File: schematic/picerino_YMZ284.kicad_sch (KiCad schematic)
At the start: 23 parts, among them CON1 PICERINO-EDGE, J1 Conn_01x02, J2 Conn_01x02, J3 Conn_01x02, U1 sn76489an, U2 74LS00, U3 LM386, Y1 3.579545Mhz

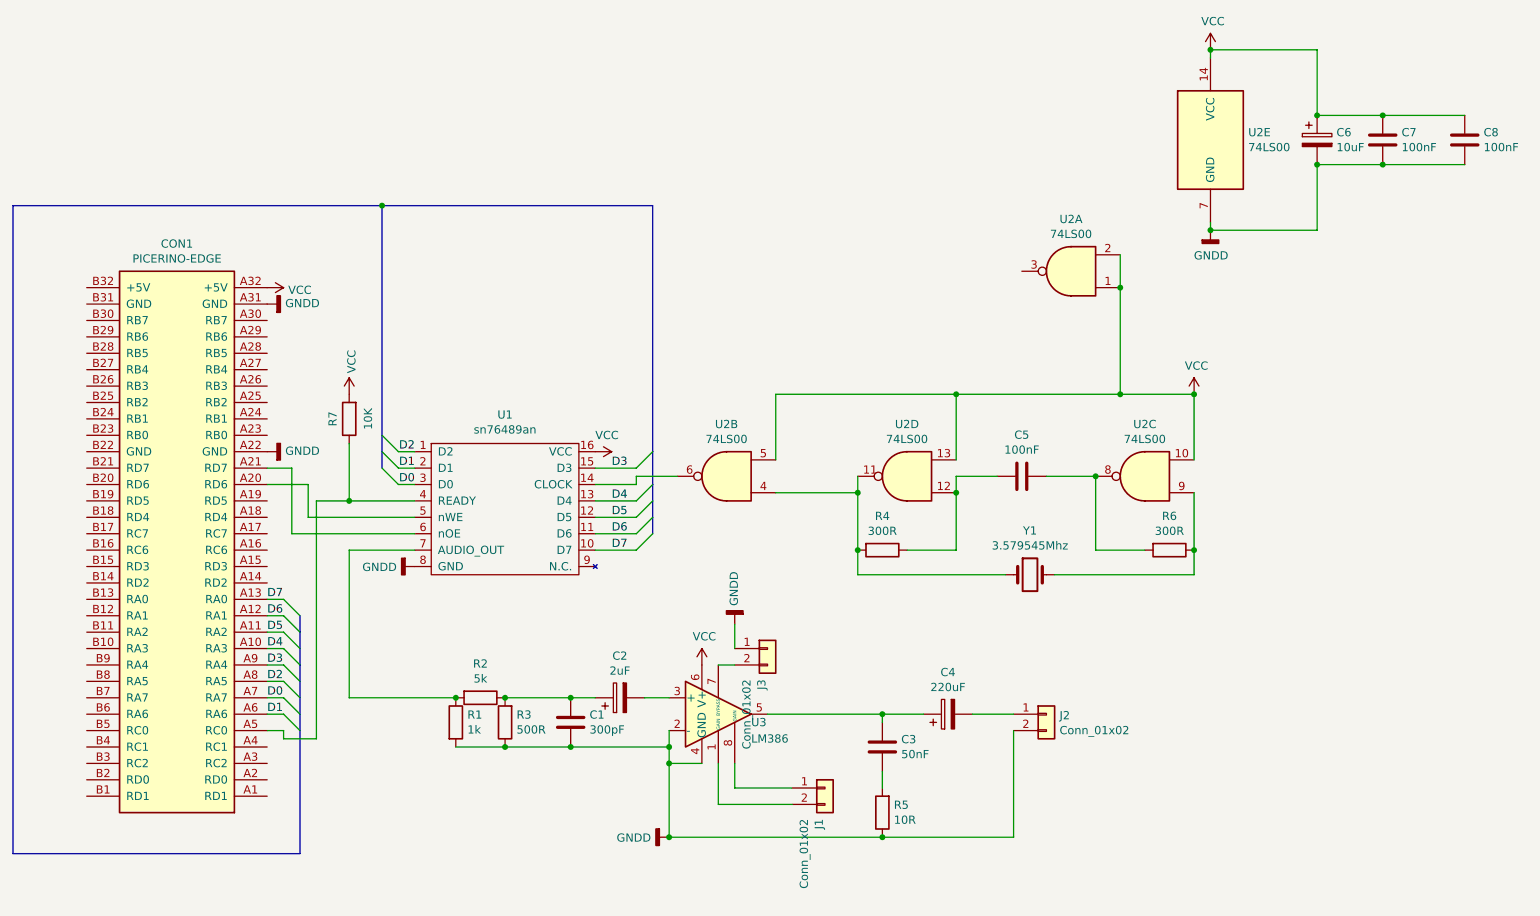
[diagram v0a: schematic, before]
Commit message: first update to YMZ284 from TI sound chip
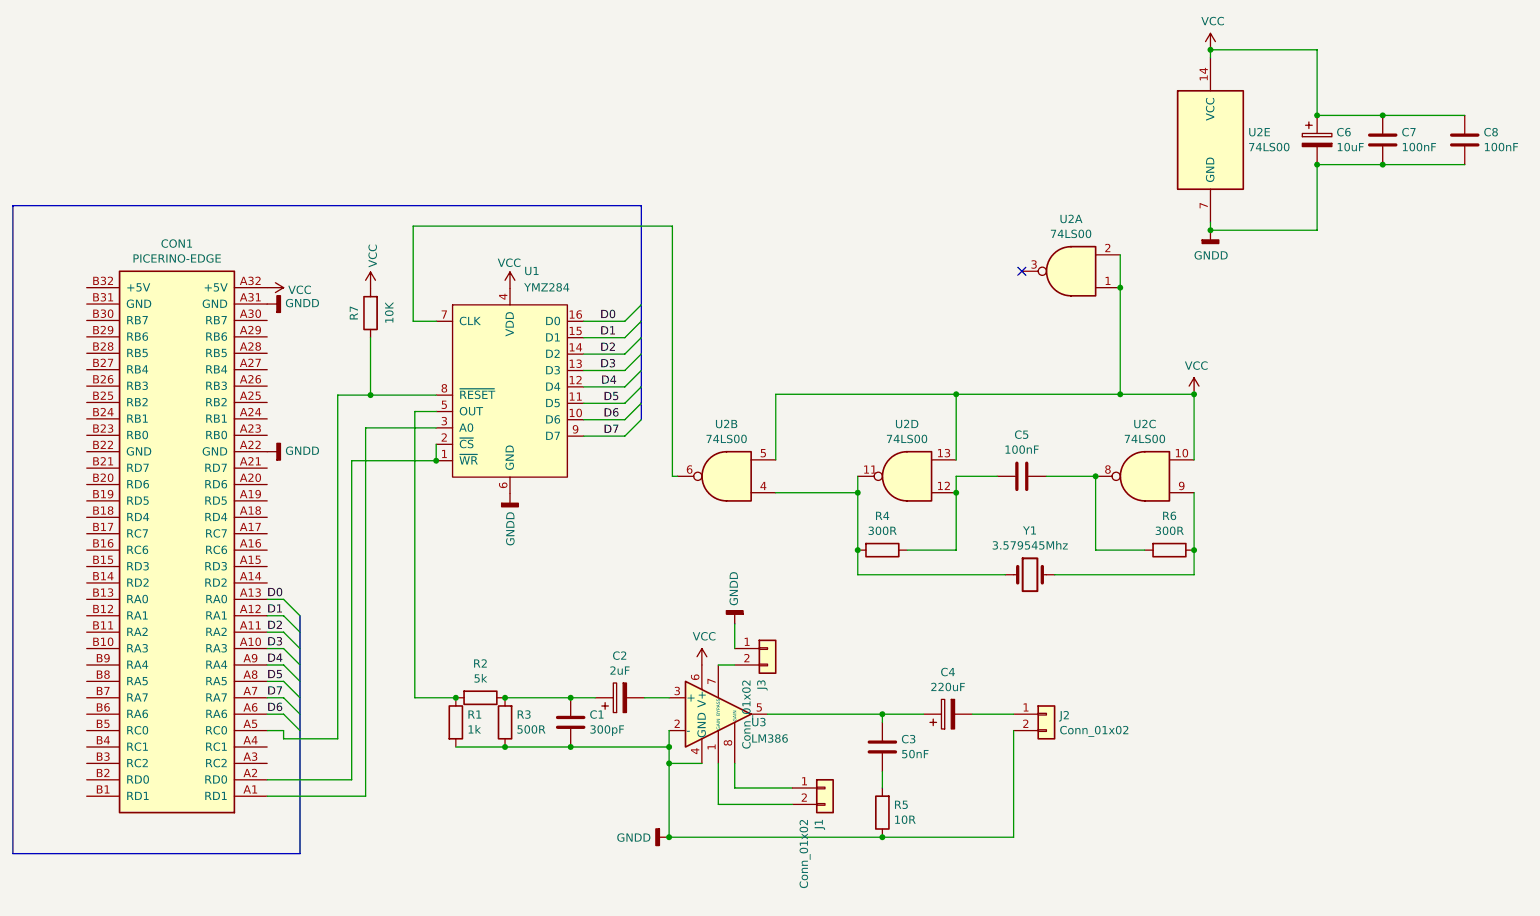
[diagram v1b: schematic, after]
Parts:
- removed U1: sn76489an, Package_DIP:DIP-16_W7.62mm_LongPads, symbol picerino_sn76489AN-rescue:sn76489an-Vintage_PC_Audio
- added U1: YMZ284, Package_DIP:DIP-16_W7.62mm_LongPads, symbol Vintage_Audio_Synth:YMZ284
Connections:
- net D0: now also CON1.A13 (RA0), U1.16 (D0); no longer CON1.A7 (RA7)
- net D1: now also CON1.A12 (RA1), U1.15 (D1); no longer CON1.A6 (RA6)
- net D2: now also CON1.A11 (RA2), U1.14 (D2); no longer CON1.A8 (RA5)
- net D3: now also CON1.A10 (RA3), U1.13 (D3); no longer CON1.A9 (RA4)
- net D4: now also CON1.A9 (RA4), U1.12 (D4); no longer CON1.A10 (RA3)
- net D5: now also CON1.A8 (RA5), U1.11 (D5); no longer CON1.A11 (RA2)
- net D6: now also CON1.A6 (RA6), U1.10 (D6); no longer CON1.A12 (RA1)
- net D7: now also CON1.A7 (RA7), U1.9 (D7); no longer CON1.A13 (RA0)
- net GNDD: now also U1.6 (GND)
- net VCC: now also U1.4 (VDD)
- net at U2.6: now also U1.7 (CLK)
- net at CON1.A5 (RC0), R7.1: now also U1.8 (~{RESET})
- net at R1.1, R2.2: now also U1.5 (OUT)
- net at CON1.A1 (RD1): now also U1.3 (A0)
- net at CON1.A2 (RD0): now also U1.1 (~{WR}), U1.2 (~{CS})
- no-connect marks 0 -> 1
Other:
- moved on the sheet: R7
